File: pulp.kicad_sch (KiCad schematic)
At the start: 0 parts

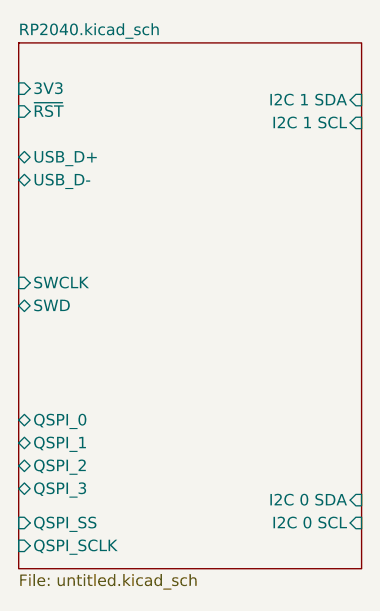
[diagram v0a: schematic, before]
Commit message: exposes proper GPIO
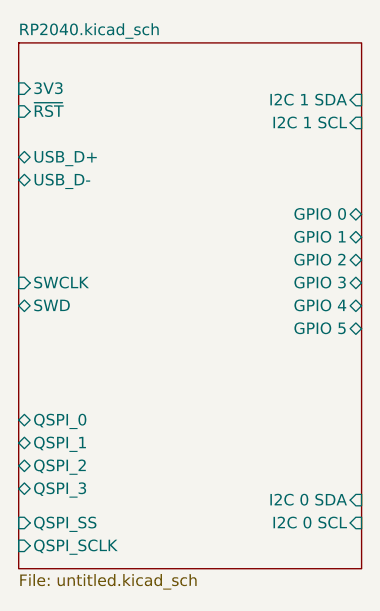
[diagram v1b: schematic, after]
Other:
- sheet RP2040.kicad_sch ports: added GPIO 0, GPIO 1, GPIO 2, GPIO 3, GPIO 4, GPIO 5; removed none
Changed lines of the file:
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@@
+      (effects (font (size 1.27 1.27)) (justify right))
+    )
+    (pin "GPIO 4" bidirectional (at 96.52 52.07 0)
+      (effects (font (size 1.27 1.27)) (justify right))
+    )
+    (pin "GPIO 1" bidirectional (at 96.52 44.45 0)
+      (effects (font (size 1.27 1.27)) (justify right))
+    )
+    (pin "GPIO 2" bidirectional (at 96.52 46.99 0)
+      (effects (font (size 1.27 1.27)) (justify right))
+    )
+    (pin "GPIO 3" bidirectional (at 96.52 49.53 0)
+      (effects (font (size 1.27 1.27)) (justify right))
+    )
+    (pin "GPIO 5" bidirectional (at 96.52 54.61 0)
+      (effects (font (size 1.27 1.27)) (justify right))
+    )
+    (pin "GPIO 0" bidirectional (at 96.52 41.91 0)
       (effects (font (size 1.27 1.27)) (justify right))
     )

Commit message: adds 2 new PWM PINS for the Motors
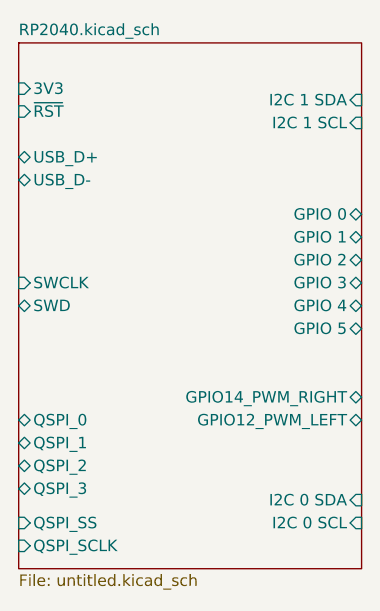
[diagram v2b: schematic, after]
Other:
- sheet RP2040.kicad_sch ports: added GPIO12_PWM_LEFT, GPIO14_PWM_RIGHT; removed none
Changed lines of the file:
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@@
+      (effects (font (size 1.27 1.27)) (justify right))
+    )
+    (pin "GPIO14_PWM_RIGHT" bidirectional (at 96.52 62.23 0)
+      (effects (font (size 1.27 1.27)) (justify right))
+    )
+    (pin "GPIO12_PWM_LEFT" bidirectional (at 96.52 64.77 0)
       (effects (font (size 1.27 1.27)) (justify right))
     )
